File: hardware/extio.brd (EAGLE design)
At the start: 100 x 80 mm, 45 parts, among them IC1 PCF8574P, Q1 IRLZ44N, Q2 IRLZ44N, Q3 IRLZ44N, Q4 IRLZ44N, Q5 IRLZ44N, Q6 IRLZ44N, Q7 IRLZ44N, Q8 IRLZ44N

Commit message: extio board
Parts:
- added C4: 1uF, resistor:TT2D4
- added U$1, U$2, U$3, U$4: (no value), gate433:3,0
- D1, D2, D3, D4, D5, D6, D7, D8: device gate433:ZDIO-5 -> gate433:SOD80C
- Q1, Q2, Q3, Q4, Q5, Q6, Q7, Q8: device gate433:TO220BH -> gate433:TO220V
- R1, R10, R11, R12, R13, R14, R15, R16, R2, R3, R4, R5, R6, R7, R8, R9: device resistor:0204/5 -> resistor:R0603
- moved Q8 56.9 mm to (50.7, 13.6)
- moved OK8 53.7 mm to (23.1, 10.7), turned to 270 degrees
- moved RN1 48.7 mm to (11.4, 43.7), turned to 270 degrees
- moved OK7 47.8 mm to (23.1, 15.7), turned to 270 degrees
- moved X1 47.3 mm to (62.0, 29.0), turned to 270 degrees
- moved Q7 45.6 mm to (50.7, 18.7)
- moved IC1 44.3 mm to (8.89, 19.6), turned to 270 degrees
- moved D8 41.1 mm to (44.2, 12.4), flipped to the bottom
- moved Q1 40.9 mm to (50.7, 49.2)
- moved R16 39.0 mm to (45.0, 9.91), flipped to the bottom, turned to 180 degrees
- moved R8 37.2 mm to (39.6, 18.8), flipped to the bottom, turned to 180 degrees
- moved OK6 37.2 mm to (23.1, 20.8), turned to 270 degrees
- moved JP1 35.9 mm to (4.24, 42.2)
- moved Q6 35.0 mm to (50.7, 23.8)
- moved R15 33.5 mm to (43.2, 15.0), flipped to the bottom, turned to 180 degrees
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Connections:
- removed net N$58: X1.10
- net +12V: now also X1.10
- net N$20: now also Q1.2; no longer Q1.D
- net N$54: now also Q1.1; no longer Q1.G
- net N$57: now also Q2.1; no longer Q2.G
- net N$60: now also Q3.1; no longer Q3.G
- net N$61: now also Q4.1; no longer Q4.G
- net N$62: now also Q5.1; no longer Q5.G
- net N$63: now also Q6.1; no longer Q6.G
- net N$65: now also Q7.1; no longer Q7.G
- net N$66: now also Q8.1; no longer Q8.G
- net N$67: now also Q2.2; no longer Q2.D
- net N$69: now also C4.+
- net N$71: now also C4.-
- net N$72: now also Q3.2; no longer Q3.D
- net N$77: now also Q4.2; no longer Q4.D
- net N$81: now also Q5.2; no longer Q5.D
- net N$85: now also Q6.2; no longer Q6.D
- net N$89: now also Q7.2; no longer Q7.D
- net N$93: now also Q8.2; no longer Q8.D
- net PE: now also Q1.3, Q2.3, Q3.3, Q4.3, Q5.3, Q6.3, Q7.3, Q8.3; no longer Q1.S, Q2.S, Q3.S, Q4.S, Q5.S, Q6.S, Q7.S, Q8.S
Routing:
- net PE: track 0.00 -> 100.1 mm
- net +12V: track 0.00 -> 50.4 mm, vias 0 -> 1
- net N$71: track 0.00 -> 42.7 mm
- net N$69: track 0.00 -> 40.4 mm, vias 0 -> 1
- net N$66: track 0.00 -> 36.8 mm
- net N$65: track 0.00 -> 35.6 mm
- net N$46: track 0.00 -> 35.2 mm
- net N$54: track 0.00 -> 34.1 mm
- net N$57: track 0.00 -> 32.9 mm
- net N$45: track 0.00 -> 32.7 mm
- net N$63: track 0.00 -> 32.0 mm
- net N$44: track 0.00 -> 30.1 mm
- net N$60: track 0.00 -> 30.1 mm
- net N$62: track 0.00 -> 29.1 mm
- net N$43: track 0.00 -> 29.1 mm
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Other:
- board size 100 x 80 mm -> 66 x 58 mm

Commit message: extio.brd, mainboard.brd, gate433.lib
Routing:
- added copper zone on layer 1, net N$71
- added copper zone on layer 16, net N$71
- added copper zone on layer 1, net PE
- added copper zone on layer 16, net PE
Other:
- board text added: "+ -"
- board text added: "ExtIO v1.0"

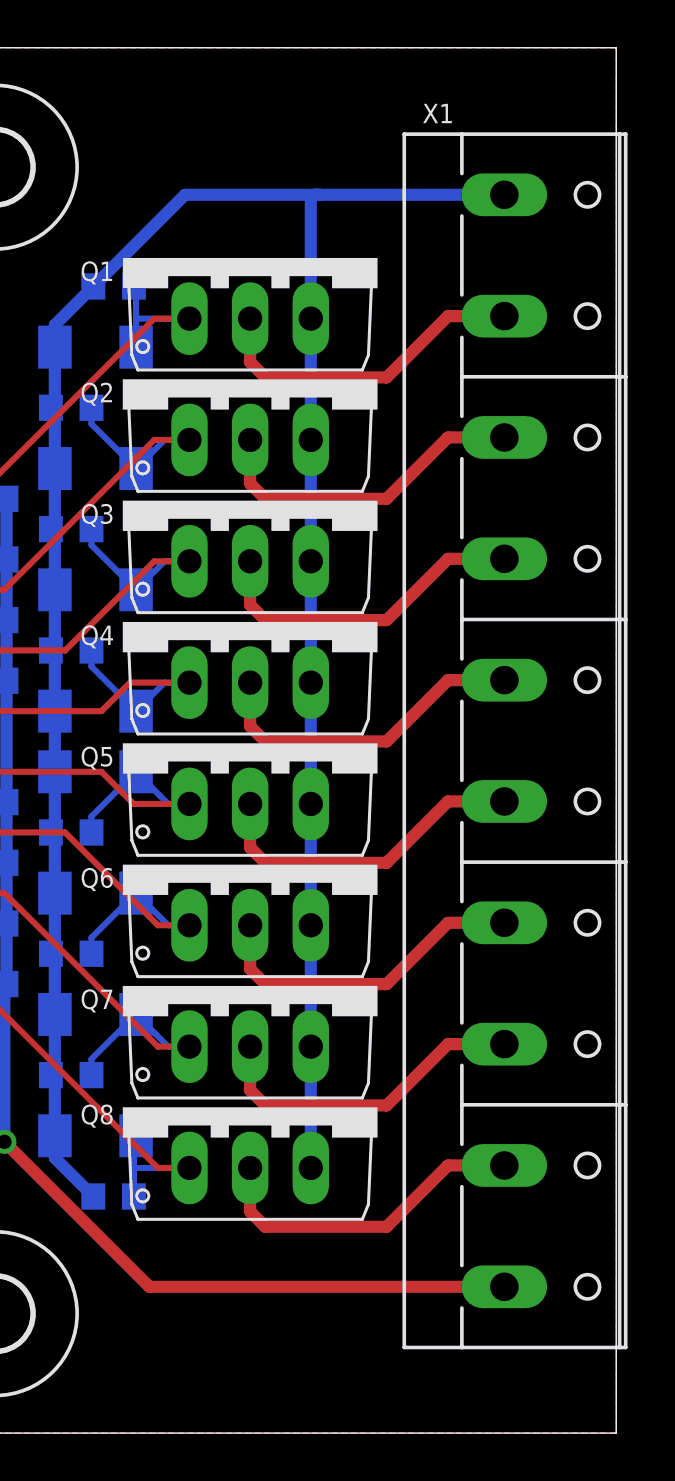
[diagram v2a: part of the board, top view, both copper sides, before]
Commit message: extio connector fix
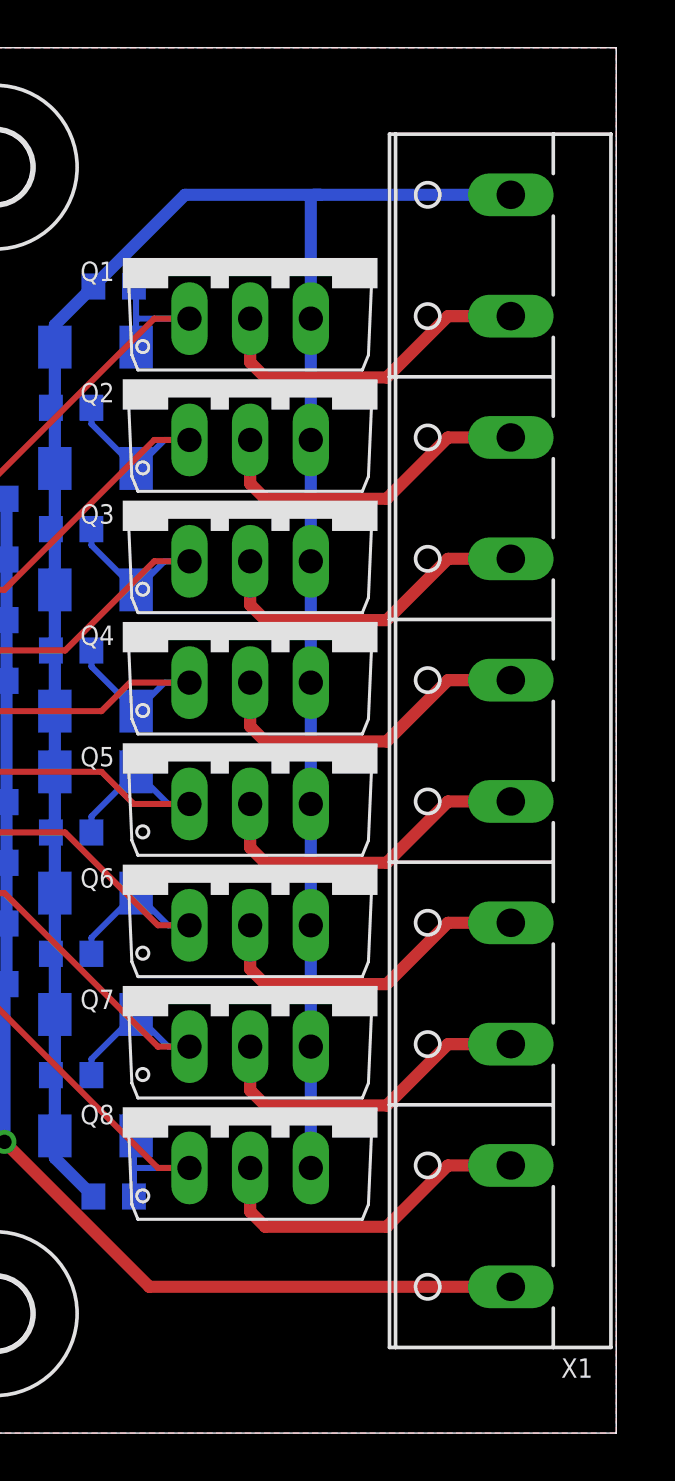
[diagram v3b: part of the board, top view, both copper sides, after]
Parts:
- moved X1 1.00 mm to (61.0, 29.0), turned to 90 degrees
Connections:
- net +12V: now also X1.1; no longer X1.10
- net N$20: now also X1.9; no longer X1.2
- net N$67: now also X1.8; no longer X1.3
- net N$72: now also X1.7; no longer X1.4
- net N$77: now also X1.6; no longer X1.5
- net N$81: now also X1.5; no longer X1.6
- net N$85: now also X1.4; no longer X1.7
- net N$89: now also X1.3; no longer X1.8
- net N$93: now also X1.2; no longer X1.9
- net PE: now also X1.10; no longer X1.1

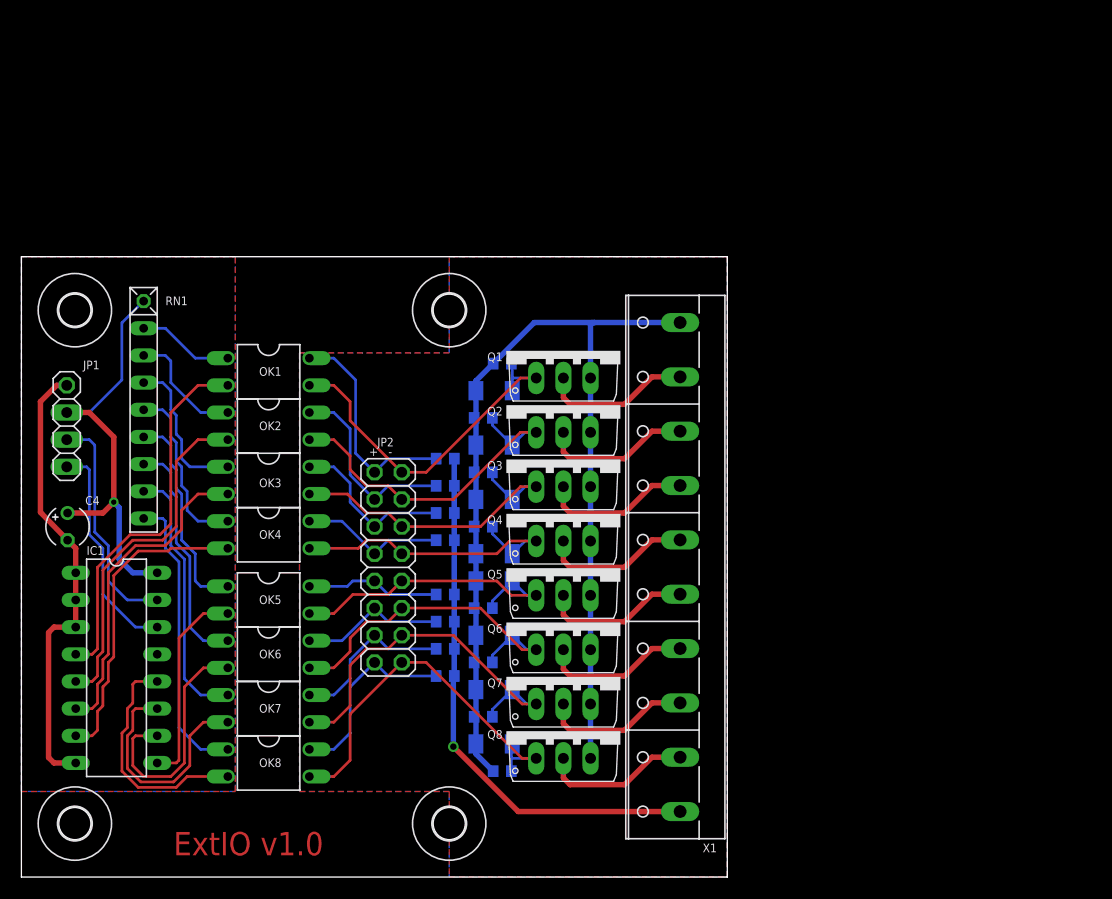
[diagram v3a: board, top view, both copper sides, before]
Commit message: extio crop and label change, mainboard label change
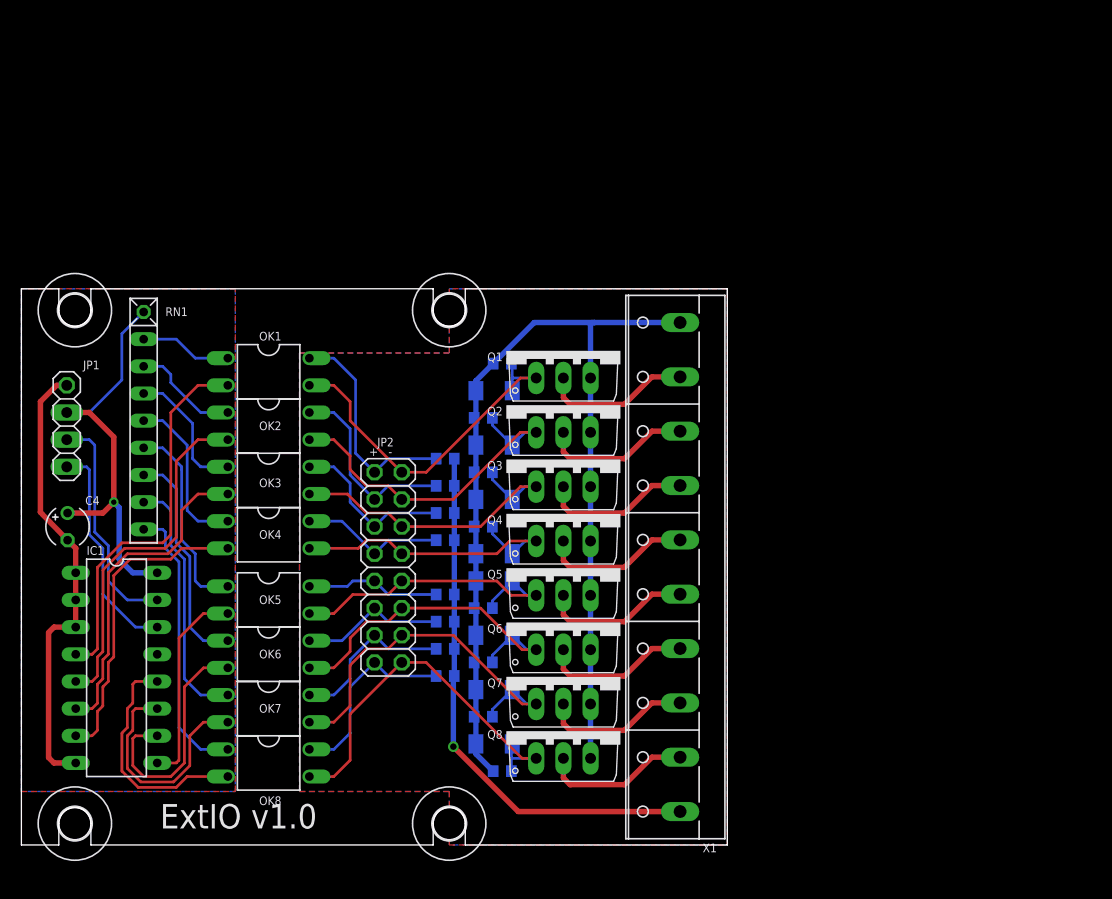
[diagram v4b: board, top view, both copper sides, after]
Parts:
- moved RN1 1.02 mm to (11.4, 42.7)
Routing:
- net N$48: track 14.3 -> 12.6 mm
- net N$47: track 11.3 -> 10.1 mm
- net N$50: track 19.8 -> 18.7 mm
- net N$49: track 16.4 -> 15.3 mm
- net N$53: track 27.4 -> 26.4 mm
- net N$52: track 24.8 -> 23.8 mm
- net N$51: track 22.2 -> 21.1 mm
- net N$69: track 40.4 -> 39.4 mm
- net N$46: track 35.2 -> 35.8 mm
- net N$44: track 30.1 -> 30.7 mm
- net N$45: track 32.7 -> 33.3 mm
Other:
- board size 66 x 58 mm -> 66 x 52 mm

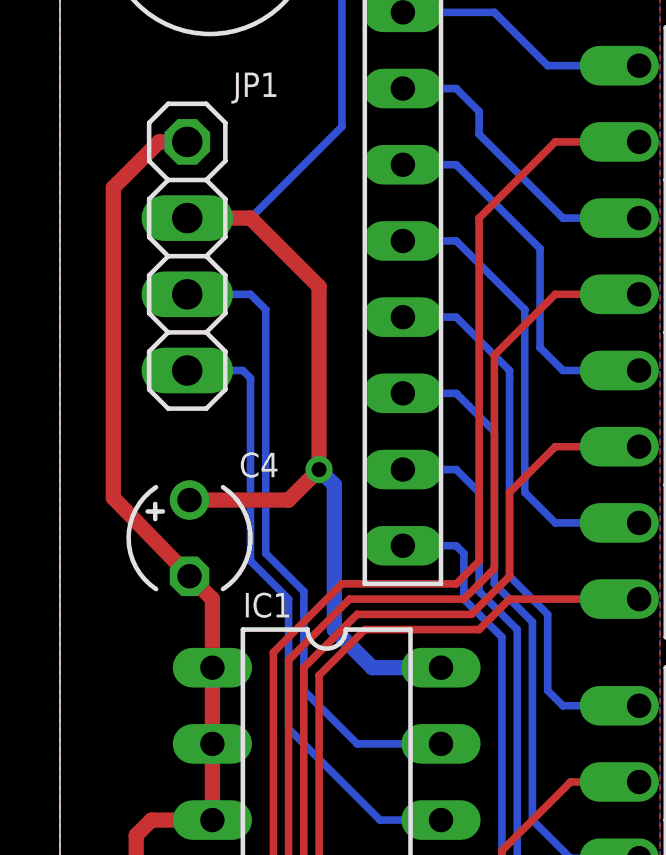
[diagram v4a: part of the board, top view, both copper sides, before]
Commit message: extio C1 to SMD
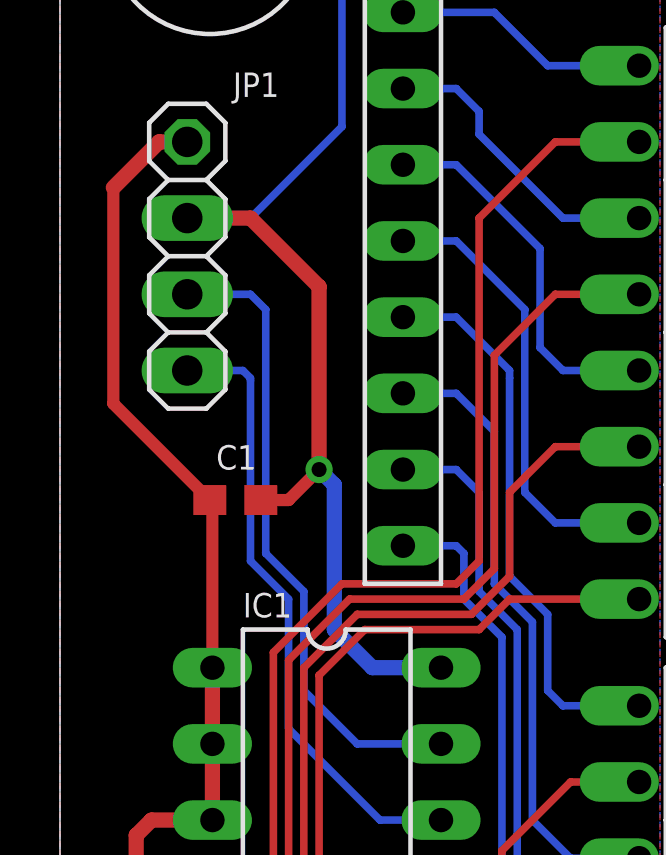
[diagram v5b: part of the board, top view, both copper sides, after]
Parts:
- removed C4: 1uF, resistor:TT2D4
- added C1: 1uF, resistor:C0603
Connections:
- net N$69: now also C1.1; no longer C4.+
- net N$71: now also C1.2; no longer C4.-
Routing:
- net N$69: track 39.4 -> 37.0 mm
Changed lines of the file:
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@@
 <setting verticaltext="up"/>
 </settings>
-<grid distance="0.5" unitdist="mm" unit="mm" style="lines" multiple="1" display="yes" altdistance="0.01" altunitdist="mm" altunit="mm"/>
+<grid distance="10" unitdist="mil" unit="mil" style="lines" multiple="1" display="yes" altdistance="1" altunitdist="mil" altunit="mil"/>
 <layers>
 <layer number="1" name="Top" color="4" fill="1" visible="yes" active="yes"/>
+<layer number="2" name="Route2" color="1" fill="3" visible="no" active="no"/>
+<layer number="3" name="Route3" color="4" fill="3" visible="no" active="no"/>
+<layer number="4" name="Route4" color="1" fill="4" visible="no" active="no"/>
+<layer number="5" name="Route5" color="4" fill="4" visible="no" active="no"/>
+<layer number="6" name="Route6" color="1" fill="8" visible="no" active="no"/>
+<layer number="7" name="Route7" color="4" fill="8" visible="no" active="no"/>
+<layer number="8" name="Route8" color="1" fill="2" visible="no" active="no"/>
+<layer number="9" name="Route9" color="4" fill="2" visible="no" active="no"/>
+<layer number="10" name="Route10" color="1" fill="7" visible="no" active="no"/>
+<layer number="11" name="Route11" color="4" fill="7" visible="no" active="no"/>
+<layer number="12" name="Route12" color="1" fill="5" visible="no" active="no"/>
+<layer number="13" name="Route13" color="4" fill="5" visible="no" active="no"/>
+<layer number="14" name="Route14" color="1" fill="6" visible="no" active="no"/>
+<layer number="15" name="Route15" color="4" fill="6" visible="no" active="no"/>
 <layer number="16" name="Bottom" color="1" fill="1" visible="yes" active="yes"/>
 <layer number="17" name="Pads" color="2" fill="1" visible="yes" active="yes"/>
@@
 <layer number="45" name="Holes" color="7" fill="1" visible="no" active="yes"/>
 <layer number="46" name="Milling" color="3" fill="1" visible="no" active="yes"/>
-<layer number="47" name="Measures" color="7" fill="1" visible="no" active="yes"/>
+<layer number="47" name="Measures" color="7" fill="1" visible="yes" active="yes"/>
 <layer number="48" name="Document" color="7" fill="1" visible="no" active="yes"/>
 <layer number="49" name="Reference" color="7" fill="1" visible="no" active="yes"/>
@@
 <element name="U$3" library="gate433" package="3,0" value="" x="40" y="5" locked="yes" smashed="yes"/>
 <element name="U$4" library="gate433" package="3,0" value="" x="40" y="53" locked="yes" smashed="yes"/>
-<element name="C4" library="resistor" package="TT2D4" value="1uF" x="4.318" y="32.766" smashed="yes" rot="R270">
-<attribute name="NAME" x="5.969" y="34.798" size="0.8128" layer="25" font="vector" ratio="10"/>
-<attribute name="VALUE" x="2.413" y="30.607" size="1.27" layer="27" ratio="10" rot="R270"/>
+<element name="C1" library="resistor" package="C0603" value="1uF" x="5.842" y="34.036" smashed="yes" rot="R180">
+<attribute name="NAME" x="5.207" y="35.052" size="0.8128" layer="25" font="vector" ratio="10"/>
+<attribute name="VALUE" x="3.683" y="35.941" size="1.27" layer="27" ratio="10" rot="R180"/>
+<attribute name="SPICEPREFIX" value="C" x="5.842" y="34.036" size="1.778" layer="27" rot="R180" display="off"/>
 </element>
 </elements>
@@
 <contactref element="RN1" pad="1"/>
 <contactref element="IC1" pad="16"/>
-<contactref element="C4" pad="+"/>
+<contactref element="C1" pad="1"/>
 <wire x1="9.398" y1="46.482" x2="6.35" y2="43.434" width="0.254" layer="16"/>
 <wire x1="6.35" y1="43.434" x2="4.2418" y2="43.434" width="0.254" layer="16"/>
@@
 <wire x1="8.636" y1="41.148" x2="6.35" y2="43.434" width="0.508" layer="1"/>
 <wire x1="6.35" y1="43.434" x2="4.2418" y2="43.434" width="0.508" layer="1"/>
-<wire x1="4.318" y1="34.036" x2="7.62" y2="34.036" width="0.508" layer="1"/>
-<wire x1="7.62" y1="34.036" x2="8.636" y2="35.052" width="0.508" layer="1"/>
+<wire x1="6.692" y1="34.036" x2="7.62" y2="34.036" width="0.4064" layer="1"/>
+<wire x1="7.62" y1="34.036" x2="8.636" y2="35.052" width="0.4064" layer="1"/>
 </signal>
 <signal name="N$71">
@@
 <contactref element="IC1" pad="8"/>
 <contactref element="JP1" pad="1"/>
-<contactref element="C4" pad="-"/>
+<contactref element="C1" pad="2"/>
 <wire x1="4.2418" y1="45.974" x2="3.302" y2="45.974" width="0.508" layer="1"/>
 <wire x1="3.302" y1="45.974" x2="1.778" y2="44.45" width="0.508" layer="1"/>
-<wire x1="1.778" y1="44.45" x2="1.778" y2="34.1094" width="0.508" layer="1"/>
-<wire x1="1.778" y1="34.1094" x2="4.318" y2="31.496" width="0.508" layer="1"/>
-<wire x1="5.08" y1="28.448" x2="5.08" y2="30.734" width="0.508" layer="1"/>
-<wire x1="5.08" y1="30.734" x2="4.318" y2="31.496" width="0.508" layer="1"/>
 <wire x1="5.08" y1="28.448" x2="5.08" y2="25.908" width="0.508" layer="1"/>
 <wire x1="5.08" y1="25.908" x2="5.08" y2="23.368" width="0.508" layer="1"/>
@@
 <vertex x="20" y="8"/>
 </polygon>
+<wire x1="1.778" y1="44.45" x2="1.778" y2="37.25" width="0.4064" layer="1"/>
+<wire x1="1.778" y1="37.25" x2="4.992" y2="34.036" width="0.4064" layer="1"/>
+<wire x1="5.08" y1="28.448" x2="5.08" y2="33.948" width="0.4064" layer="1"/>
+<wire x1="5.08" y1="33.948" x2="4.992" y2="34.036" width="0.4064" layer="1"/>
 </signal>
 </signals>
